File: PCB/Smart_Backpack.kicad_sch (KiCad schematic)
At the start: 9 parts, among them U3 ESP32-PICO-MINI-02-N8R2

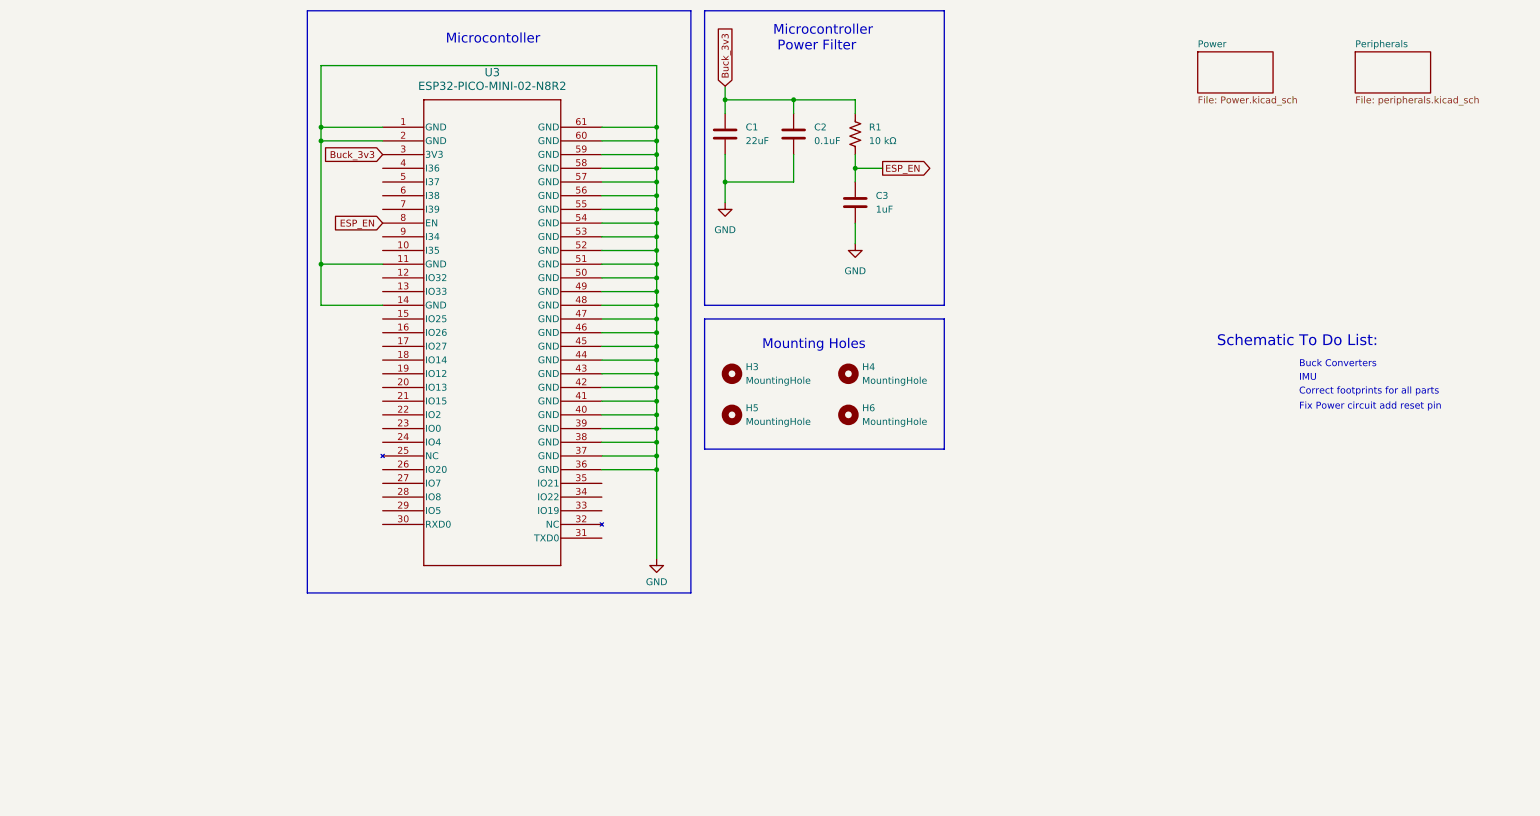
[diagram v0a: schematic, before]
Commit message: Work on adding on board flashing
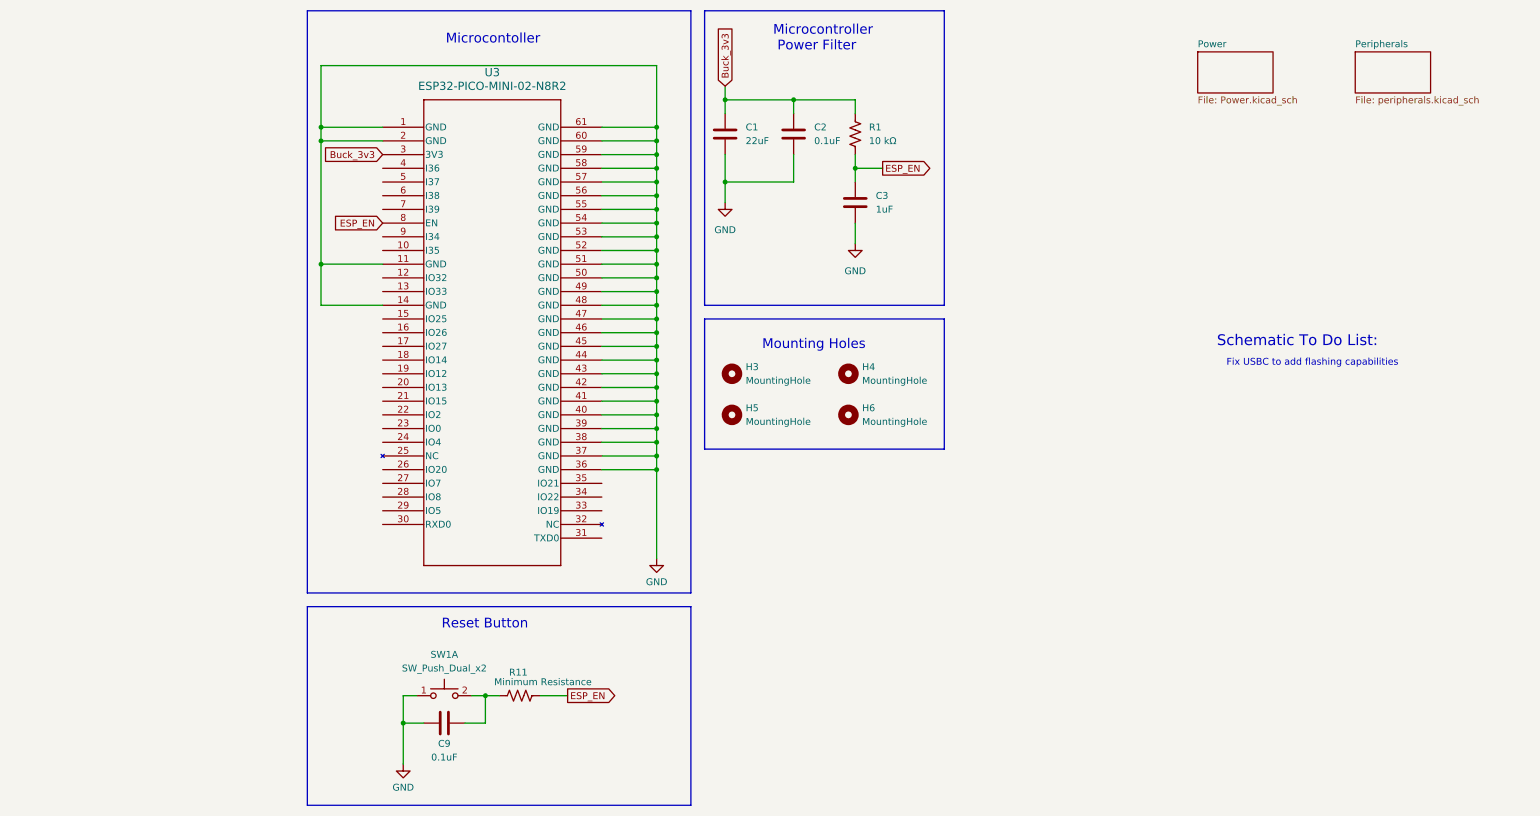
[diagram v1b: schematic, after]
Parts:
- added C9: 0.1uF, Capacitor_SMD:C_1206_3216Metric_Pad1.33x1.80mm_HandSolder, symbol Device:C
- added R11: Minimum Resistance, Resistor_SMD:R_1206_3216Metric_Pad1.30x1.75mm_HandSolder, symbol Device:R_US
- added SW1: SW_Push_Dual_x2, symbol Switch:SW_Push_Dual_x2
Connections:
- net ESP_EN: now also R11.2
- net GND: now also C9.2, SW1.1 (C)
- new net: C9.1, R11.1, SW1.2 (D)
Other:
- note added: "Fix USBC to add flashing capabilities"
- note added: "Reset Button"
- note removed: "Buck Converters"
- note removed: "Correct footprints for all parts"
- note removed: "Fix Power circuit add reset pin"
- note removed: "IMU"

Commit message: Updated to-do list
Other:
- note added: "Add testing leds"
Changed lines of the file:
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@@
+		)
+	)
+	(text "Add testing leds"
+		(exclude_from_sim no)
+		(at 184.658 82.804 0)
+		(effects
+			(font
+				(size 1.27 1.27)
+			)
+			(justify left bottom)
 		)
 	)

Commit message: Created push button footprint
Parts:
- SW1: footprint (none) -> SMD_Button:Shop_SMD_Button
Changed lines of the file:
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@@
 			)
 		)
-		(property "Footprint" ""
+		(property "Footprint" "SMD_Button:Shop_SMD_Button"
 			(at 39.37 135.89 0)
 			(effects

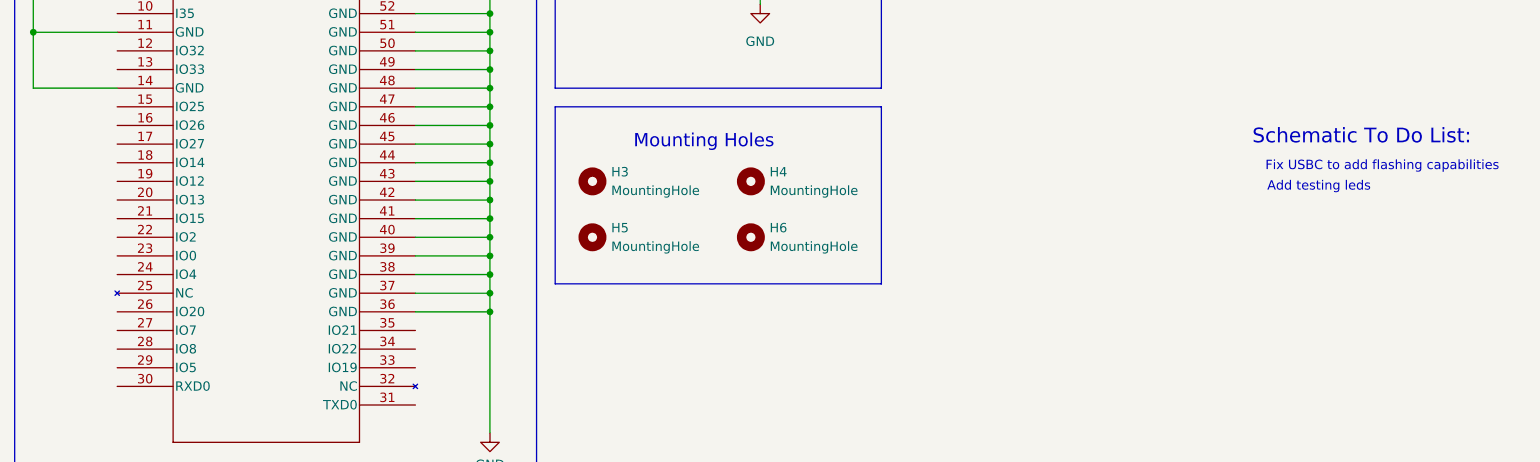
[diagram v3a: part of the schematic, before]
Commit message: Added IO0 button
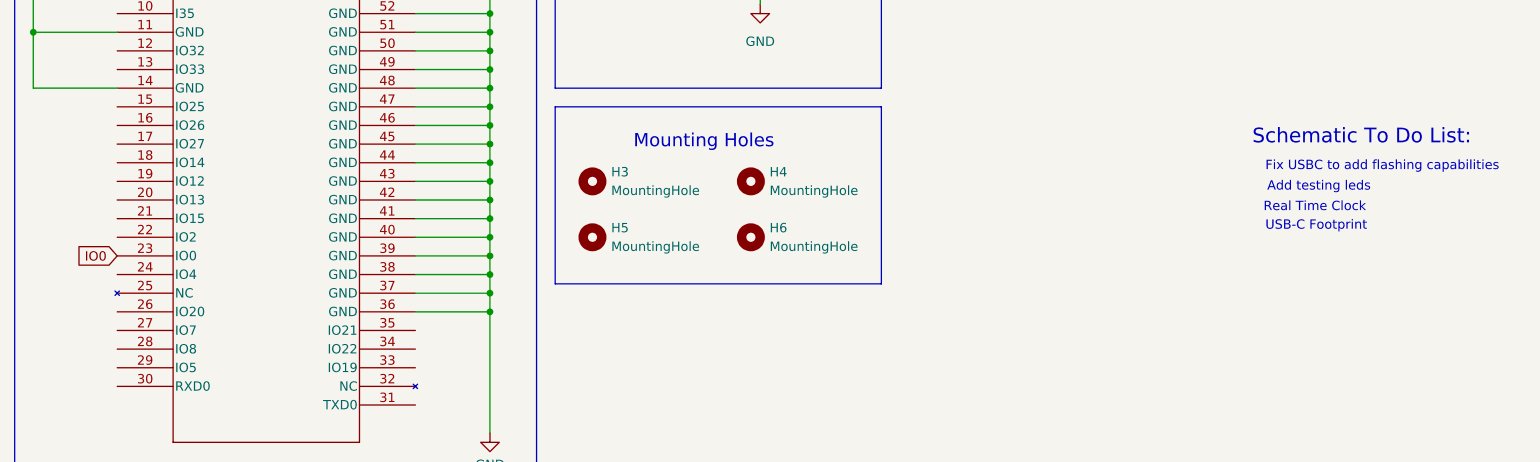
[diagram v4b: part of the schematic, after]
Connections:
- net IO0: now reaches U3.23 (IO0)
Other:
- note added: "Real Time Clock"
- note added: "USB-C Footprint"
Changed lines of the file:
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@@
+		)
+	)
+	(text "Real Time Clock"
+		(exclude_from_sim no)
+		(at 184.15 85.598 0)
+		(effects
+			(font
+				(size 1.27 1.27)
+			)
+			(justify left bottom)
 		)
 	)
@@
 		)
 	)
+	(text "USB-C Footprint"
+		(exclude_from_sim no)
+		(at 184.404 88.138 0)
+		(effects
+			(font
+				(size 1.27 1.27)
+			)
+			(justify left bottom)
+		)
+	)
 	(text "Schematic To Do List:"
 		(exclude_from_sim no)
@@
 		)
 	)
-	(text "Fix USBC to add flashing capabilities"
+	(text "Fix USBC to add flashing capabilities\n"
 		(exclude_from_sim no)
 		(at 184.404 80.01 0)
@@
 				(hide yes)
 			)
+		)
+	)
+	(global_label "IO0"
+		(shape input)
+		(at 27.94 91.44 180)
+		(fields_autoplaced yes)
+		(effects
+			(font
+				(size 1.27 1.27)
+			)
+			(justify right)
+		)
+		(property "Intersheetrefs" "${INTERSHEET_REFS}"
+			(at 21.81 91.44 0)
+			(effects
+				(font
+					(size 1.27 1.27)
+				)
+				(justify right)
+				(hide yes)
+			)

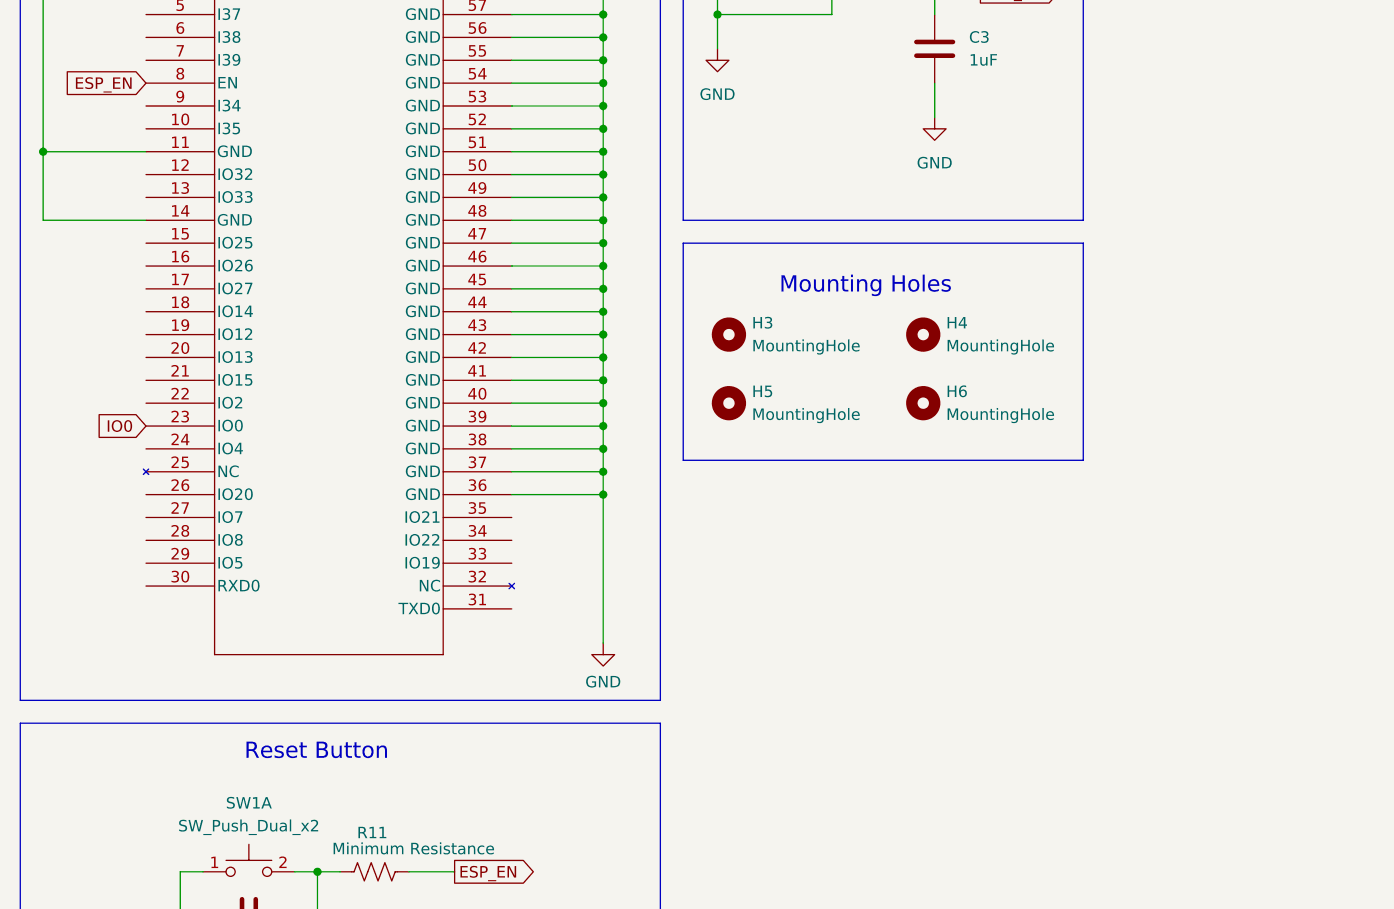
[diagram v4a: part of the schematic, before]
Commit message: add RTC and TX/RX signals
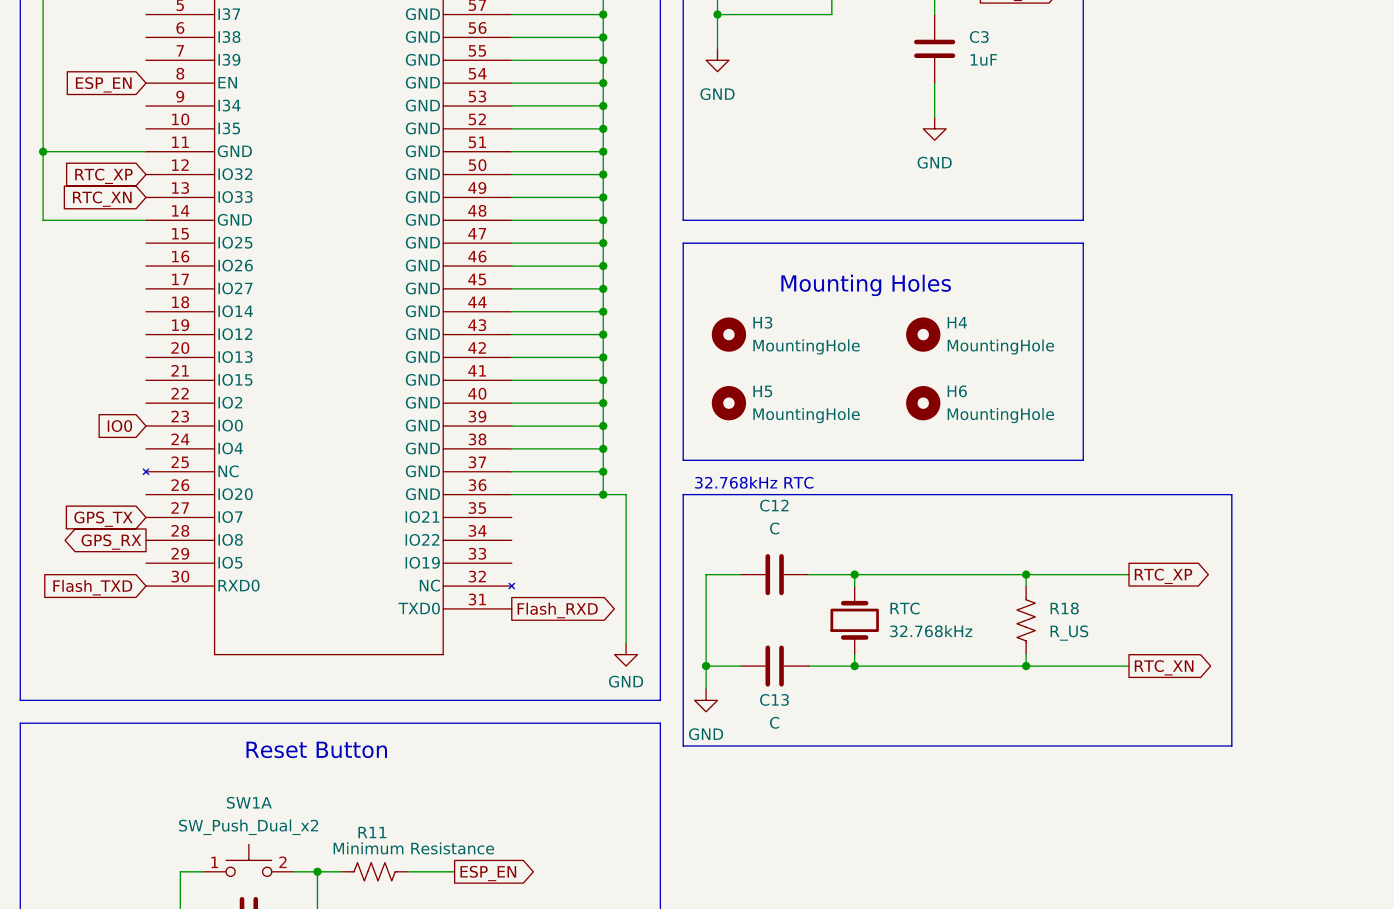
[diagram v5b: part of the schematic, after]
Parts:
- added C12, C13: C, symbol Device:C
- added R18: R_US, symbol Device:R_US
- added RTC: 32.768kHz, symbol Device:Crystal
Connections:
- net GND: now also C12.1, C13.1
- net RTC_XP: now reaches U3.12 (IO32)
- net RTC_XP: now also C12.2, R18.1, RTC.2
- net RTC_XN: now reaches U3.13 (IO33)
- net RTC_XN: now also C13.2, R18.2, RTC.1
- net GPS_TX: now reaches U3.27 (IO7)
- net GPS_RX: now reaches U3.28 (IO8)
- net Flash_TXD: now reaches U3.30 (RXD0)
- net Flash_RXD: now reaches U3.31 (TXD0)
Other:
- note added: "32.768kHz RTC"

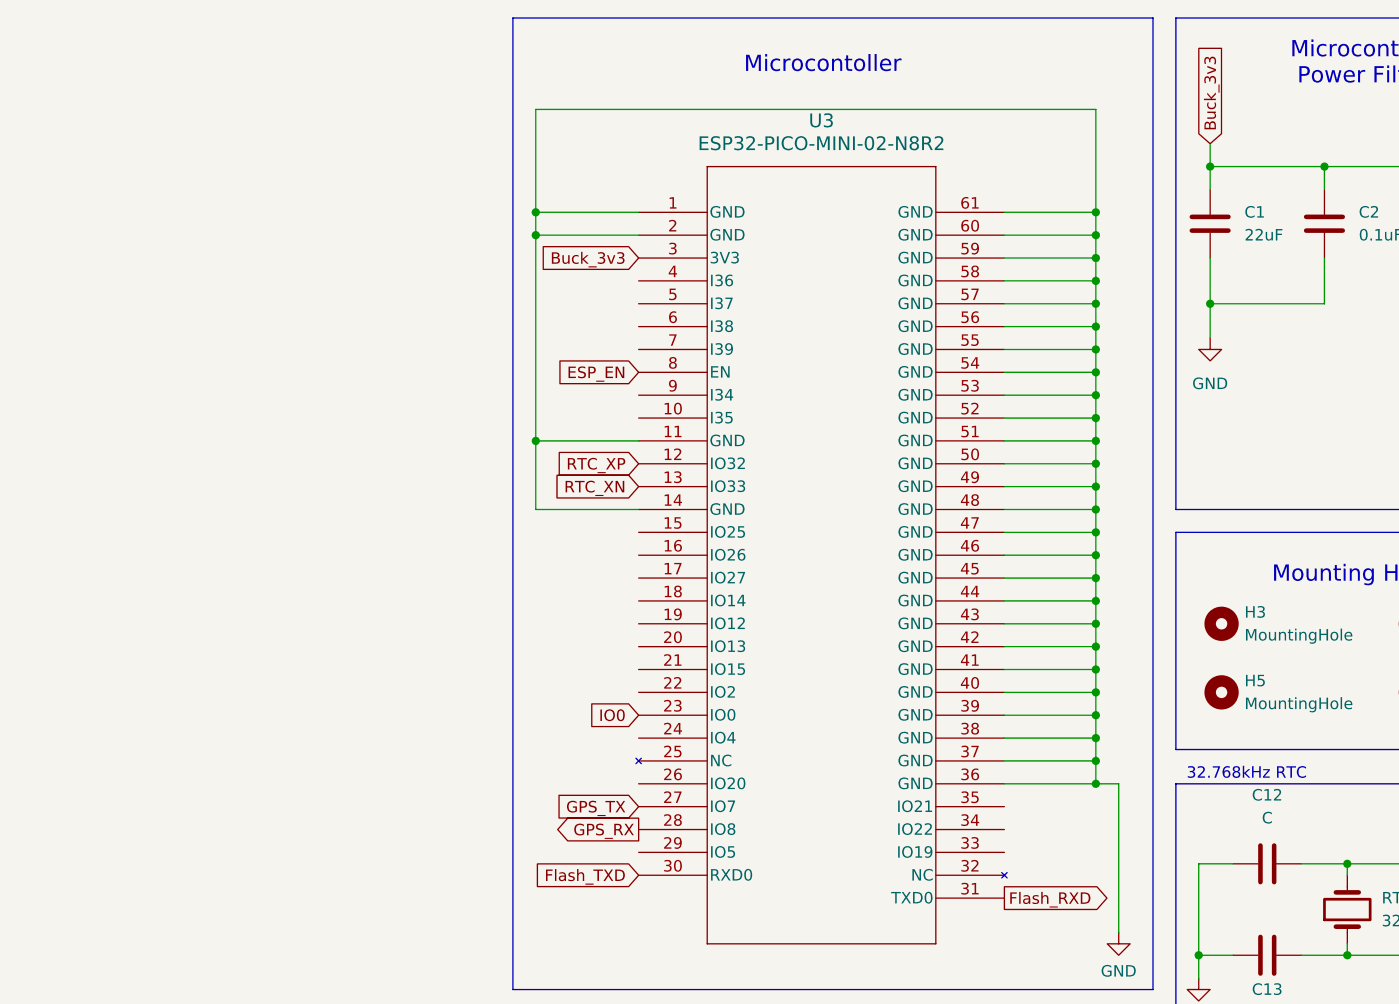
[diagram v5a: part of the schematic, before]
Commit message: add power indicator LEDs, connect peripherals
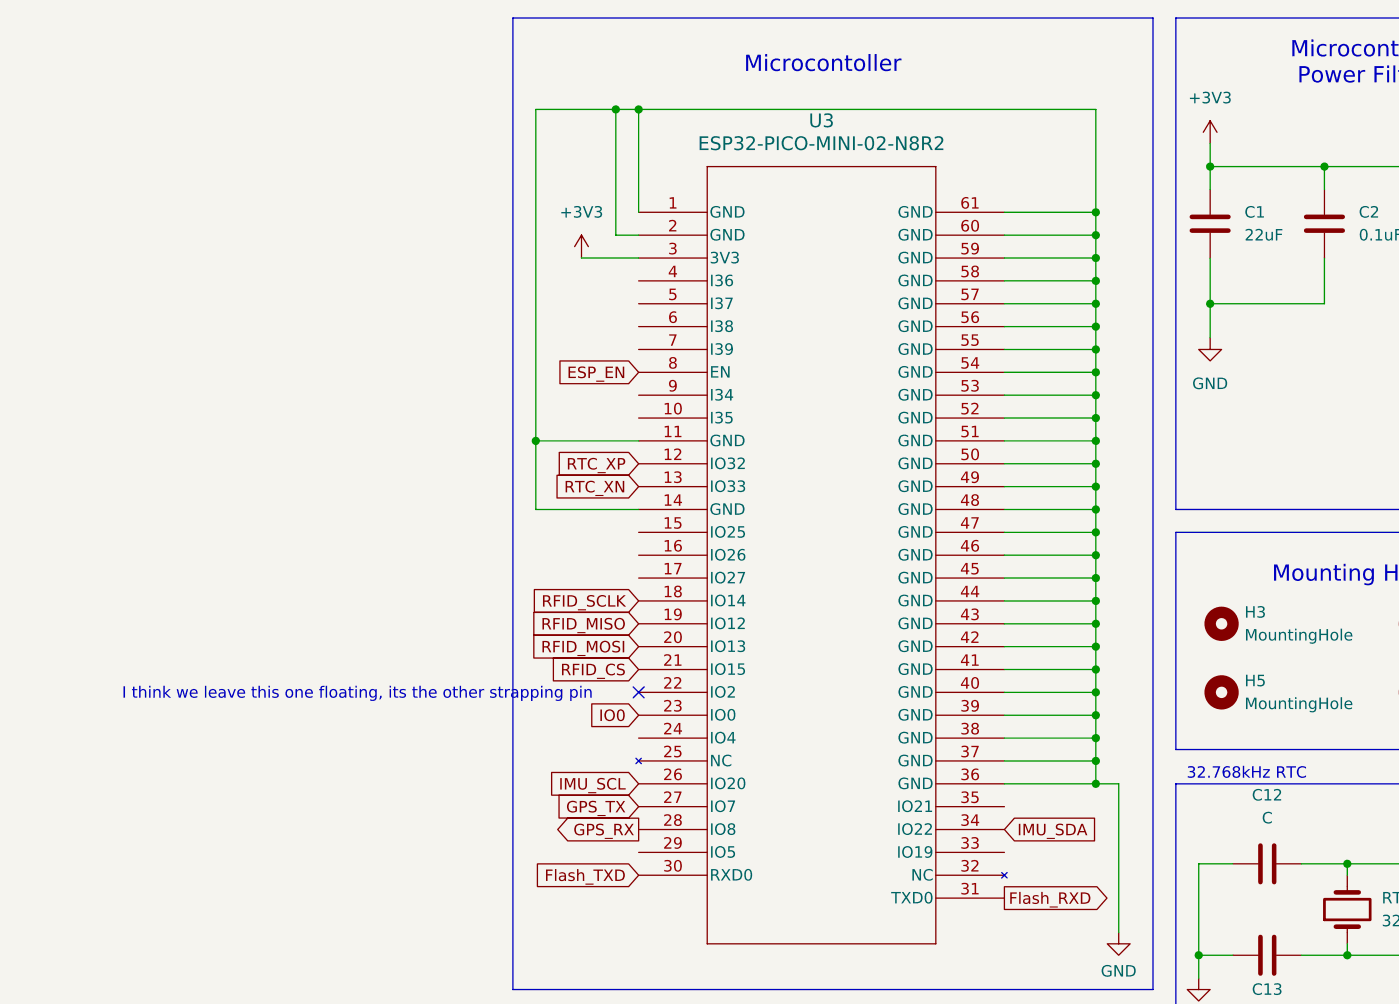
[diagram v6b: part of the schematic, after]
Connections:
- net RFID_SCLK: now reaches U3.18 (IO14)
- net RFID_MISO: now reaches U3.19 (IO12)
- net RFID_MOSI: now reaches U3.20 (IO13)
- net RFID_CS: now reaches U3.21 (IO15)
- net IMU_SCL: now reaches U3.26 (IO20)
- net IMU_SDA: now reaches U3.34 (IO22)
- net Buck_3v3 renamed +3V3
- no-connect marks 0 -> 1
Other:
- note added: "I think we leave this one floating, its the other strapping pin"
